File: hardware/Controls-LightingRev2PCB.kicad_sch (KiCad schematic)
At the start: 40 parts, among them IC2 TLV70433DBVT, IC3 TLV70130DBVR, J2 MX150_02x08_RightAngle, J3 53307-2471, Q2 IRLML0030, Q3 IRLML0030, U1 TLV2371DBV, U2 INA241A5xD, U3 INA241A5xD, U4 INA241A5xD, U5 SN74LV1T34DBV, U8 TLV2371DBV, U9 TLV2371DBV

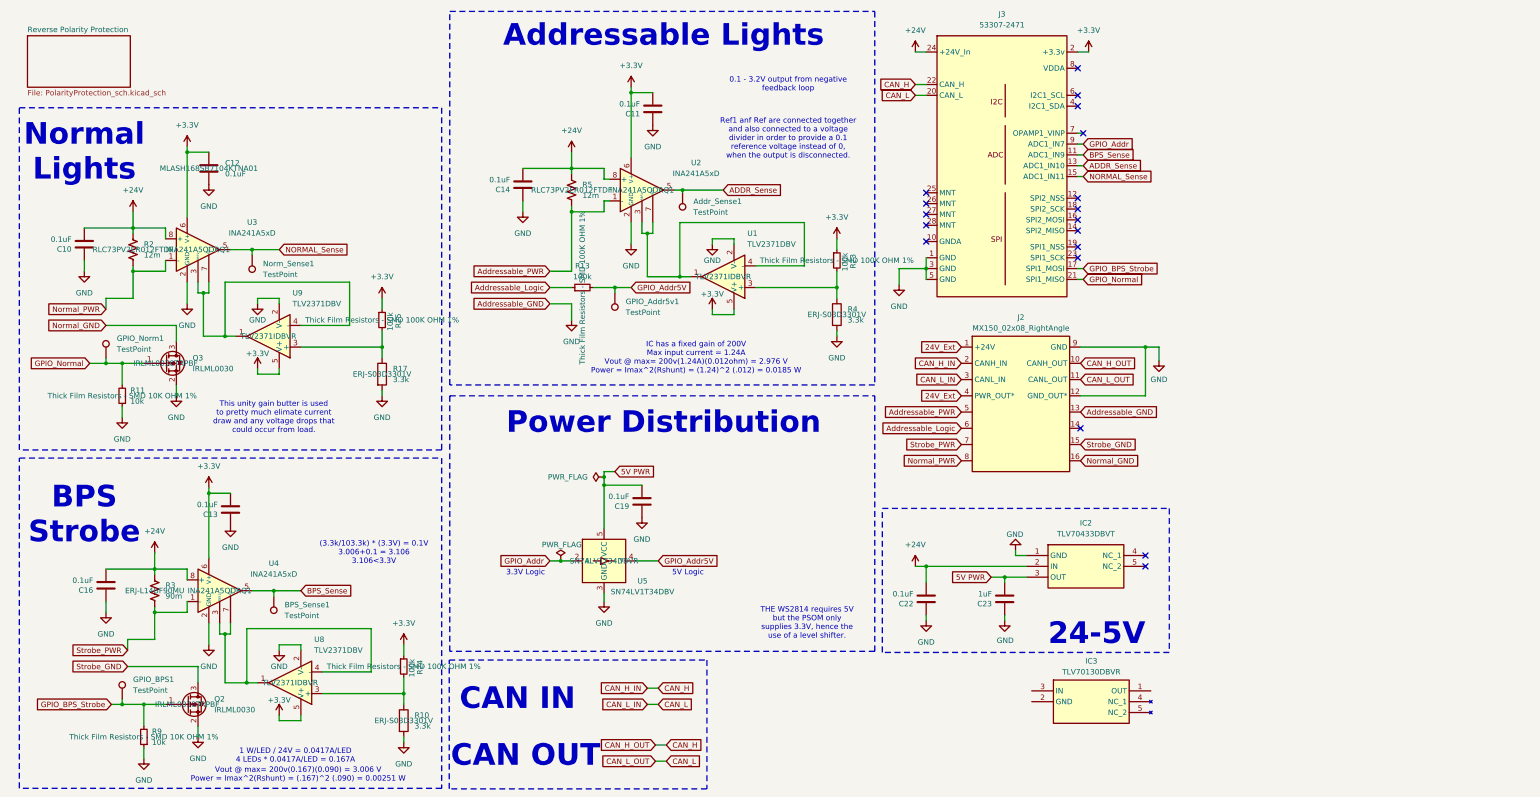
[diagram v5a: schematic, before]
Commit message: Rev B schematic Review for correct SOM connector and new IC
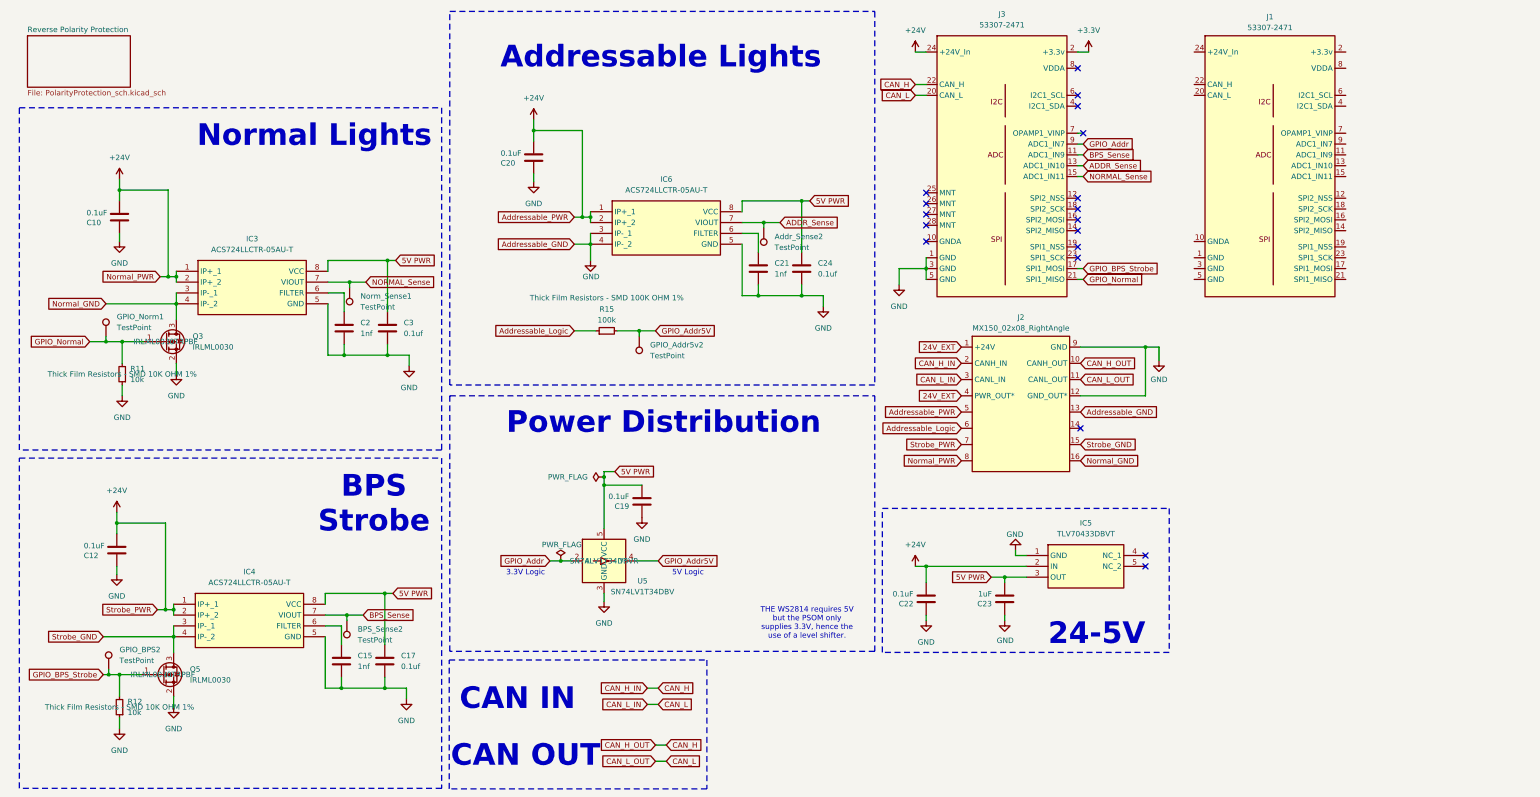
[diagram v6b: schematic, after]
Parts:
- removed Addr_Sense1, BPS_Sense1, GPIO_Addr5v1, GPIO_BPS1: TestPoint, UTSVT_Special:TestPoint_HEX_3mmID, symbol Connector:TestPoint
- removed C11, C13, C14, C16: 0.1uF, Capacitor_SMD:C_0603_1608Metric, symbol Device:C
- removed IC2: TLV70433DBVT, SOT95P280X145-5N, symbol TLB70433DBVT:TLV70433DBVT
- removed IC3: TLV70130DBVR, UTSVT_Power:TLV70130DBVR, symbol UTSVT-Power:TLV70130DBVR
- removed Q2: IRLML0030, Package_TO_SOT_SMD:SOT-23, symbol Transistor_FET:IRLML0030
- removed R10, R17, R4: 3.3k, Resistor_SMD:R_0603_1608Metric, symbol Device:R
- removed R13, R23, R24, R25: 100k, Resistor_SMD:R_0603_1608Metric, symbol Device:R_Small
- removed R2, R5: 12m, Resistor_SMD:R_1206_3216Metric_Pad1.30x1.75mm_HandSolder, symbol Device:R_US
- removed R3: 90m, Resistor_SMD:R_1206_3216Metric_Pad1.30x1.75mm_HandSolder, symbol Device:R_US
- removed R9: 10k, Resistor_SMD:R_0603_1608Metric, symbol Device:R_Small
- removed U1, U8, U9: TLV2371DBV, Package_TO_SOT_SMD:SOT-23-5, symbol Amplifier_Operational:TLV2371DBV
- removed U2, U3, U4: INA241A5xD, Package_SO:SOIC-8_3.9x4.9mm_P1.27mm, symbol Amplifier_Current:INA241A5xD
- added Addr_Sense2, BPS_Sense2, GPIO_Addr5v2, GPIO_BPS2: TestPoint, UTSVT_Special:TestPoint_HEX_3mmID, symbol Connector:TestPoint
- added C15, C2, C21: 1nf, symbol Device:C
- added C17, C24, C3: 0.1uf, symbol Device:C
- added C20: 0.1uF, Capacitor_SMD:C_0603_1608Metric, symbol Device:C
- added IC3, IC4, IC6: ACS724LLCTR-05AU-T, Lighting_IC:SOIC127P600X175-8N, symbol ACS724LLCTR:ACS724LLCTR-05AU-T
- added IC5: TLV70433DBVT, Lighting_Board:SOT95P280X145-5N, symbol TLB70433DBVT:TLV70433DBVT
- added J1: 53307-2471, UTSVT_Connectors:PeripheralSOM, symbol UTSVT-Connectors:PeripheralSOMConnector
- added Q5: IRLML0030, Package_TO_SOT_SMD:SOT-23, symbol Transistor_FET:IRLML0030
- added R12: 10k, Resistor_SMD:R_0603_1608Metric, symbol Device:R_Small
- added R15: 100k, Resistor_SMD:R_0603_1608Metric, symbol Device:R_Small
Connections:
- net Addressable_PWR is gone; now on net +24V: J2.5
- net Normal_PWR is gone; now on net +24V: J2.8
- net Strobe_PWR is gone; now on net +24V: J2.7
- net +24V: now also C12.2, C20.2, IC3.1 (IP+_1), IC3.2 (IP+_2), IC4.1 (IP+_1), IC4.2 (IP+_2), IC5.2 (IN), IC6.1 (IP+_1), IC6.2 (IP+_2)
- net +3.3V: no longer C12.2
- net 5V PWR: now also C17.1, C24.1, C3.1, IC3.8 (VCC), IC4.8 (VCC), IC5.3 (OUT), IC6.8 (VCC)
- net ADDR_Sense: now also Addr_Sense2.1, IC6.7 (VIOUT)
- net Addressable_Logic: now also R15.1
- net BPS_Sense: now also BPS_Sense2.1, IC4.7 (VIOUT)
- net GND: now also C15.2, C17.2, C2.2, C20.1, C21.2, C24.2, C3.2, IC3.5 (GND), IC4.5 (GND), IC5.1 (GND), IC6.3 (IP-_1), IC6.4 (IP-_2), IC6.5 (GND), Q5.2 (S), R12.1
- net GPIO_Addr5V: now also GPIO_Addr5v2.1, R15.2
- net GPIO_BPS_Strobe: now also GPIO_BPS2.1, Q5.1 (G), R12.2
- net NORMAL_Sense: now also IC3.7 (VIOUT)
- net Normal_GND: now also IC3.3 (IP-_1), IC3.4 (IP-_2)
- net Strobe_GND: now also IC4.3 (IP-_1), IC4.4 (IP-_2), Q5.3 (D)
- net 24V_Ext renamed 24V_EXT
- new net: C2.1, IC3.6 (FILTER)
- new net: C21.1, IC6.6 (FILTER)
- new net: C15.1, IC4.6 (FILTER)
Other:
- note removed: "(3.3k/103.3k) * (3.3V) = 0.1V 3.006+0.1 = 3.106 3.106<3.3V"
- note removed: "0.1 - 3.2V output from negative feedback loop"
- note removed: "1 W/LED / 24V = 0.0417A/LED 4 LEDs * 0.0417A/LED = 0.167A"
- note removed: "IC has a fixed gain of 200V Max input current = 1.24A Vout @ max= 200v(1.24A)(0.012ohm) = 2.976 V Power = Imax^2(Rshunt) = (1.24)^2 (.012) = 0.0185 W"
- note removed: "Ref1 anf Ref are connected together and also connected to a voltage divider in order to provide a 0.1 reference voltage instead of 0, when the output is disconnected."
- note removed: "This unity gain butter is used to pretty much elimate current draw and any voltage drops that could occur from load."
- note removed: "Vout @ max= 200v(0.167)(0.090) = 3.006 V Power = Imax^2(Rshunt) = (.167)^2 (.090) = 0.00251 W"
- moved on the sheet: C10, GPIO_Norm1, Norm_Sense1, Q3, R11

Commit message: Rev B schematic Review with new IC
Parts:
- removed J3: 53307-2471, UTSVT_Connectors:PeripheralSOM, symbol utsvt-connectors:PeripheralSOMConnector
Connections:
- net +24V: now also J1.24 (+24V_In)
- net +3.3V: now also J1.2 (+3.3v)
- net ADDR_Sense: now also J1.13 (ADC1_IN10)
- net BPS_Sense: now also J1.11 (ADC1_IN9)
- net CAN_H: now also J1.22 (CAN_H)
- net CAN_L: now also J1.20 (CAN_L)
- net GND: now also J1.1 (GND), J1.3 (GND), J1.5 (GND)
- net GPIO_Addr: now also J1.9 (ADC1_IN7)
- net GPIO_BPS_Strobe: now also J1.17 (SPI1_MOSI)
- net GPIO_Normal: now also J1.21 (SPI1_MISO)
- net NORMAL_Sense: now also J1.15 (ADC1_IN11)
- no-connect marks 18 -> 14
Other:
- moved on the sheet: Addr_Sense2, BPS_Sense2, C10, C12, C15, C17, C19, C2, C21, C22, C23, C24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

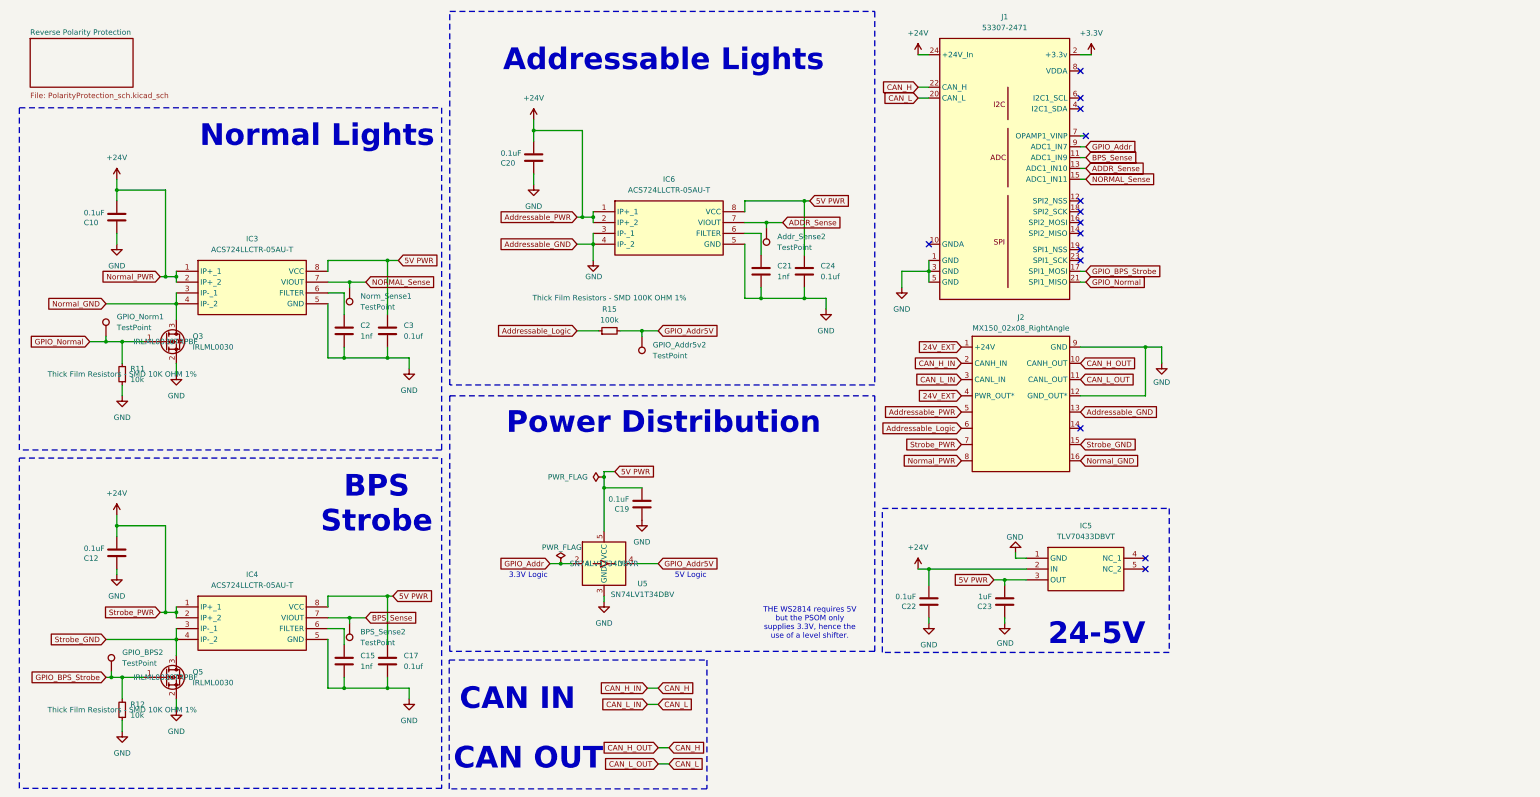
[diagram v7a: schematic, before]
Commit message: Switched MX150 to 02x05 nanofet
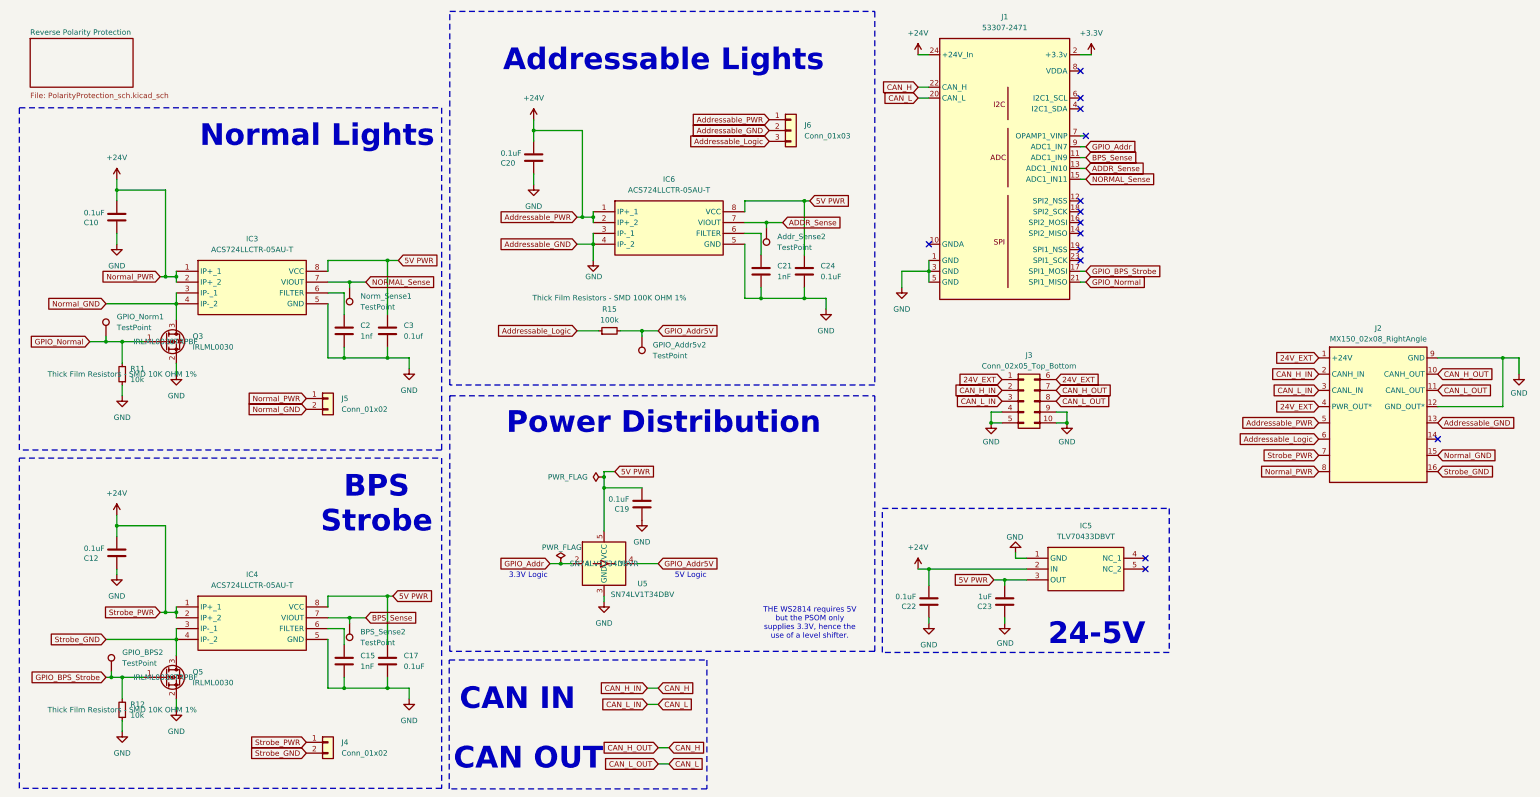
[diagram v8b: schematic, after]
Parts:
- added J3: Conn_02x05_Top_Bottom, symbol Connector_Generic:Conn_02x05_Top_Bottom
- added J4, J5: Conn_01x02, symbol Connector_Generic:Conn_01x02
- added J6: Conn_01x03, symbol Connector_Generic:Conn_01x03
- C15, C21: value 1nf -> 1nF; footprint (none) -> Capacitor_SMD:C_0603_1608Metric
- C17, C24: value 0.1uf -> 0.1uF; footprint (none) -> Capacitor_SMD:C_0603_1608Metric
- C2, C3: footprint (none) -> Capacitor_SMD:C_0603_1608Metric
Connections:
- net +24V: now also J4.1 (Pin_1), J5.1 (Pin_1), J6.1 (Pin_1)
- net 24V_EXT: now also J3.1 (Pin_1), J3.6 (Pin_6)
- net Addressable_Logic: now also J6.3 (Pin_3)
- net CAN_H: now also J3.2 (Pin_2), J3.7 (Pin_7)
- net CAN_L: now also J3.3 (Pin_3), J3.8 (Pin_8)
- net GND: now also J3.10 (Pin_10), J3.4 (Pin_4), J3.5 (Pin_5), J3.9 (Pin_9), J6.2 (Pin_2)
- net Normal_GND: now also J2.15, J5.2 (Pin_2); no longer J2.16
- net Strobe_GND: now also J2.16, J4.2 (Pin_2); no longer J2.15
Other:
- moved on the sheet: J2
